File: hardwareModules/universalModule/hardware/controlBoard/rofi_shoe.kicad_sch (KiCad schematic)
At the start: 24 parts

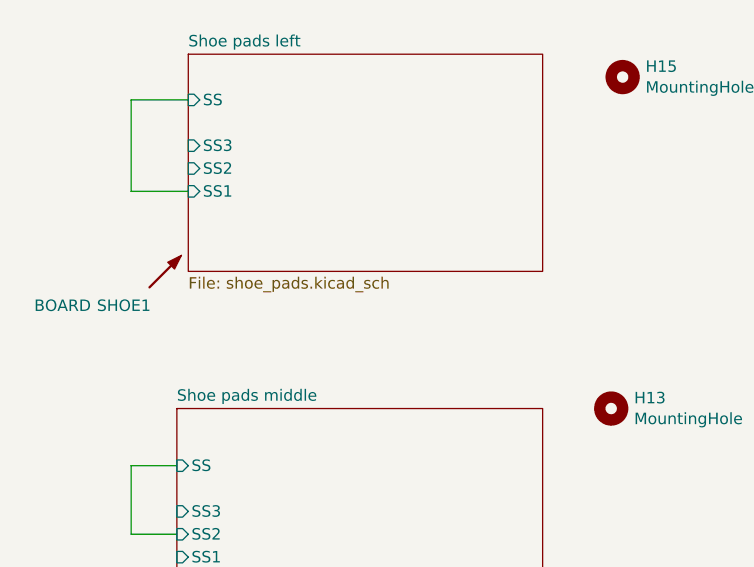
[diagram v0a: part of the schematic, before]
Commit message: um: Fix hardware bugs, prepare v0.5
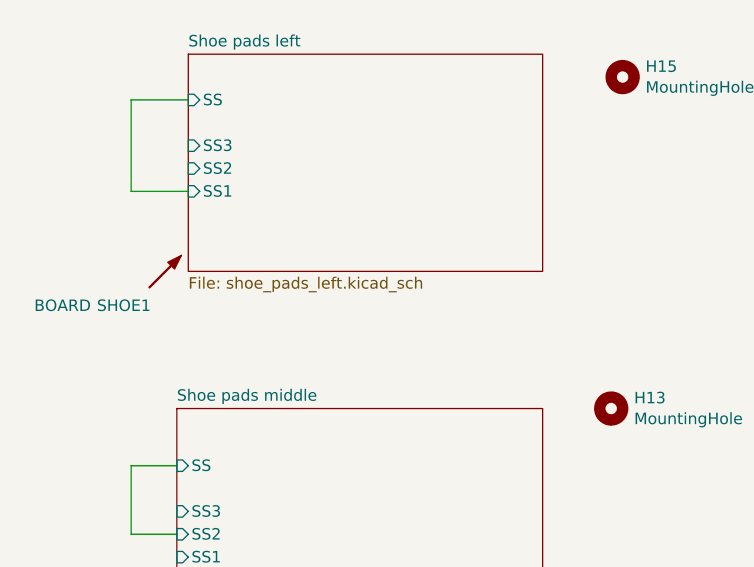
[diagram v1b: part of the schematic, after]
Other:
- sheet Shoe pads left: file shoe_pads.kicad_sch -> shoe_pads_left.kicad_sch
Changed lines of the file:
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@@
       (effects (font (size 1.27 1.27)) (justify left bottom))
     )
-    (property "Sheet file" "shoe_pads.kicad_sch" (id 1) (at 52.07 56.4646 0)
+    (property "Sheet file" "shoe_pads_left.kicad_sch" (id 1) (at 52.07 56.4646 0)
       (effects (font (size 1.27 1.27)) (justify left top))
     )
